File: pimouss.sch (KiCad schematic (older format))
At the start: 13 parts

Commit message: sch: Misc fixes
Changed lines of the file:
@@
 $Descr A4 11693 8268
 encoding utf-8
-Sheet 6 9
+Sheet 6 10
 Title "The Pimouss itself"
 Date "2019-03-19"
@@
 Text Label 3050 2000 0    50   ~ 0
 PWR_UP
-Text Label 3050 2100 0    50   ~ 0
+Text Label 3650 2100 2    50   ~ 0
 nRST
 NoConn ~ 2900 1900
@@
 Wire Wire Line
 	2900 2200 3650 2200
-Text Label 3050 2200 0    50   ~ 0
+Text Label 3650 2200 2    50   ~ 0
 nMR
 Wire Bus Line
@@
 Entry Wire Line
 	1450 1700 1550 1800
-Text Label 1100 1600 0    50   ~ 0
+Text Label 1050 1600 0    50   ~ 0
 PCIE_1X
 Wire Bus Line
@@
 Wire Bus Line
 	4150 3600 3750 3600
-Text Label 3800 3600 0    50   ~ 0
+Text Label 4150 3600 2    50   ~ 0
 PCIE_1X
 Entry Wire Line
@@
 Wire Bus Line
 	8050 2200 7650 2200
-Text Label 7700 2200 0    50   ~ 0
+Text Label 8050 2200 2    50   ~ 0
 PCIE_1X
 Entry Wire Line
@@
 Wire Bus Line
 	8050 1900 7650 1900
-Text Label 7700 1900 0    50   ~ 0
+Text Label 8050 1900 2    50   ~ 0
 PCIE_4X
 Entry Wire Line
@@
 Wire Bus Line
 	8050 3000 7650 3000
-Text Label 7700 3000 0    50   ~ 0
+Text Label 8050 3000 2    50   ~ 0
 PCIE_4X
 Entry Wire Line
@@
 Entry Wire Line
 	5350 2500 5450 2600
-Text Label 5000 2400 0    50   ~ 0
+Text Label 4950 2400 0    50   ~ 0
 PCIE_4X
 Entry Wire Line
@@
 Entry Wire Line
 	5350 4300 5450 4400
-Text Label 1100 2500 0    50   ~ 0
+Text Label 1050 2500 0    50   ~ 0
 QSGMII
 Wire Bus Line
 	4150 2200 3750 2200
-Text Label 3850 2200 0    50   ~ 0
+Text Label 4150 2200 2    50   ~ 0
 GPIO
 Entry Wire Line
@@
 Wire Bus Line
 	3750 2500 4150 2500
-Text Label 3850 2500 0    50   ~ 0
+Text Label 4150 2500 2    50   ~ 0
 MIIM
-Text Label 3850 2700 0    50   ~ 0
+Text Label 4150 2700 2    50   ~ 0
 GPIO
 NoConn ~ 2900 3200
@@
 Wire Wire Line
 	7550 1700 6800 1700
-Text Label 6950 1600 0    50   ~ 0
+Text Label 7550 1600 2    50   ~ 0
 BSTRAP_L
-Text Label 6950 1700 0    50   ~ 0
+Text Label 7550 1700 2    50   ~ 0
 BSTRAP_H
 NoConn ~ 6800 2900
@@
 Wire Bus Line
 	8050 2600 7650 2600
-Text Label 7750 2600 0    50   ~ 0
+Text Label 8050 2600 2    50   ~ 0
 UART
 Entry Wire Line
@@
 Wire Bus Line
 	8950 4100 8550 4100
-Text Label 8600 4100 0    50   ~ 0
+Text Label 8950 4100 2    50   ~ 0
 SMBUS
 Entry Wire Line
@@
 Wire Bus Line
 	8050 3400 7650 3400
-Text Label 7750 3400 0    50   ~ 0
+Text Label 8050 3400 2    50   ~ 0
 JTAG
 Entry Wire Line
@@
 Wire Bus Line
 	1900 5600 1500 5600
-Text Label 1550 5600 0    50   ~ 0
+Text Label 1900 5600 2    50   ~ 0
 PCIE_1X
 Wire Bus Line
 	1900 5700 1500 5700
-Text Label 1550 5700 0    50   ~ 0
+Text Label 1900 5700 2    50   ~ 0
 PCIE_4X
 Wire Bus Line
 	1900 5900 1500 5900
-Text Label 1550 5900 0    50   ~ 0
+Text Label 1900 5900 2    50   ~ 0
 QSGMII
 Wire Bus Line
 	1500 6000 1900 6000
-Text Label 1600 6000 0    50   ~ 0
+Text Label 1900 6000 2    50   ~ 0
 MIIM
 Wire Bus Line
 	1900 6200 1500 6200
-Text Label 1600 6200 0    50   ~ 0
+Text Label 1900 6200 2    50   ~ 0
 GPIO
 Wire Bus Line
 	1900 6300 1500 6300
-Text Label 1600 6300 0    50   ~ 0
+Text Label 1900 6300 2    50   ~ 0
 UART
 Wire Bus Line
 	1900 6400 1500 6400
-Text Label 1600 6400 0    50   ~ 0
+Text Label 1900 6400 2    50   ~ 0
 SDIO
 Wire Bus Line
 	1900 6500 1500 6500
-Text Label 1550 6500 0    50   ~ 0
+Text Label 1900 6500 2    50   ~ 0
 SMBUS
 Wire Bus Line
 	1900 6700 1500 6700
-Text Label 1600 6700 0    50   ~ 0
+Text Label 1900 6700 2    50   ~ 0
 JTAG
 Wire Wire Line
@@
 Wire Wire Line
 	1500 7000 1900 7000
-Text Label 1600 6900 0    50   ~ 0
+Text Label 1900 6900 2    50   ~ 0
 nRST
-Text Label 1600 7000 0    50   ~ 0
+Text Label 1900 7000 2    50   ~ 0
 nMR
 $Comp
@@
 Wire Wire Line
 	1500 7100 1900 7100
-Text Label 1550 7100 0    50   ~ 0
+Text Label 1900 7100 2    50   ~ 0
 BSTRAP
 $Comp
@@
 Wire Wire Line
 	6200 6100 5700 6100
-Text Label 5800 6000 0    50   ~ 0
+Text Label 6200 6000 2    50   ~ 0
 BSTRAP_L
-Text Label 5800 6100 0    50   ~ 0
+Text Label 6200 6100 2    50   ~ 0
 BSTRAP_H
 Wire Wire Line
@@
 Wire Wire Line
 	8150 3750 8200 3750
-Wire Bus Line
-	5350 2400 5350 4300
-Wire Bus Line
-	7650 3400 7650 4000
-Wire Bus Line
-	3750 2700 3750 3000
-Wire Bus Line
-	1450 2500 1450 2900
-Wire Bus Line
-	3750 2200 3750 2400
-Wire Bus Line
-	3750 3900 3750 4400
 Entry Wire Line
 	3650 4500 3750 4400
@@
 Entry Wire Line
 	3650 4200 3750 4100
-Text Label 3850 3900 0    50   ~ 0
+Text Label 4150 3900 2    50   ~ 0
 SDIO
 Wire Bus Line
@@
 Wire Wire Line
 	3650 4000 2900 4000
+Wire Bus Line
+	3750 2200 3750 2400
+Wire Bus Line
+	1450 2500 1450 2900
+Wire Bus Line
+	3750 2700 3750 3000
+Wire Bus Line
+	7650 3400 7650 4000
+Wire Bus Line
+	3750 3900 3750 4400
+Wire Bus Line
+	5350 2400 5350 4300
 $EndSCHEMATC

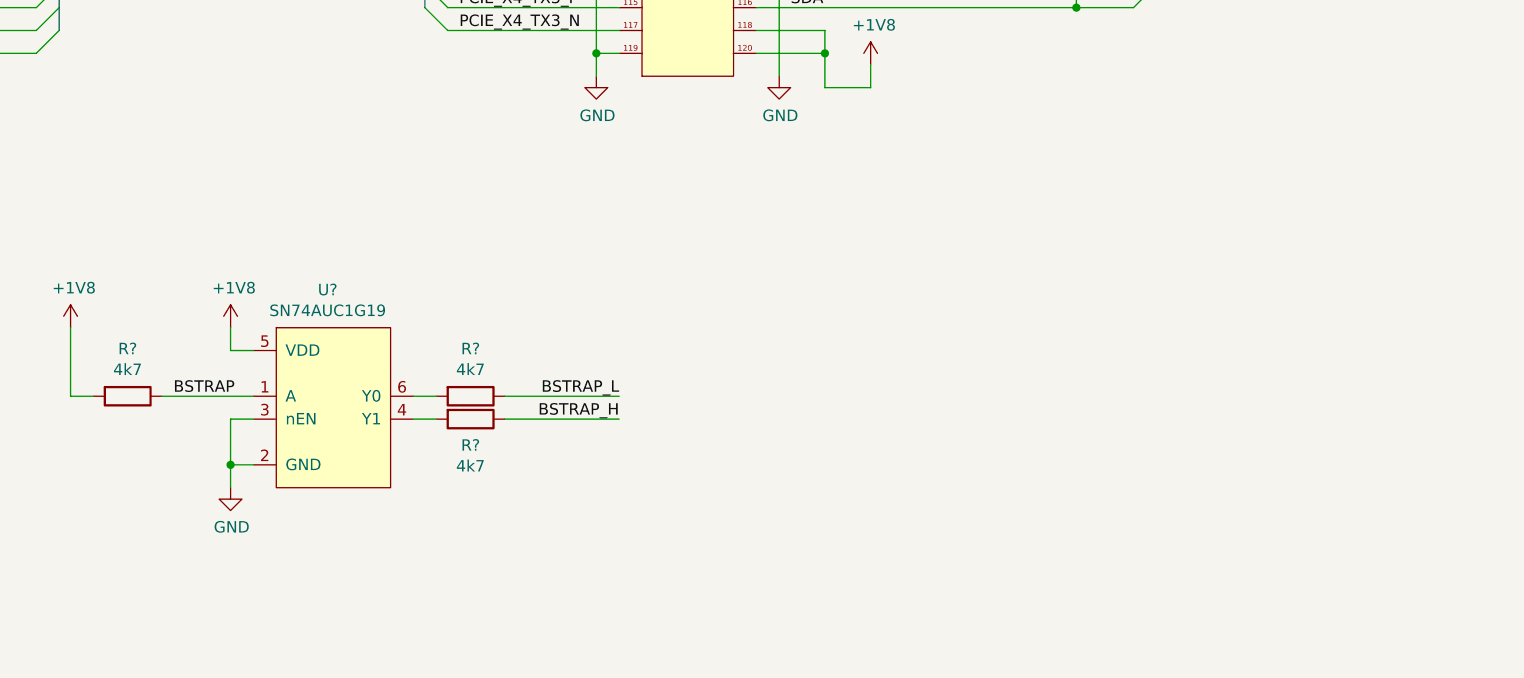
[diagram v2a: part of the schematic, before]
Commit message: sch: Add pimouss power connector
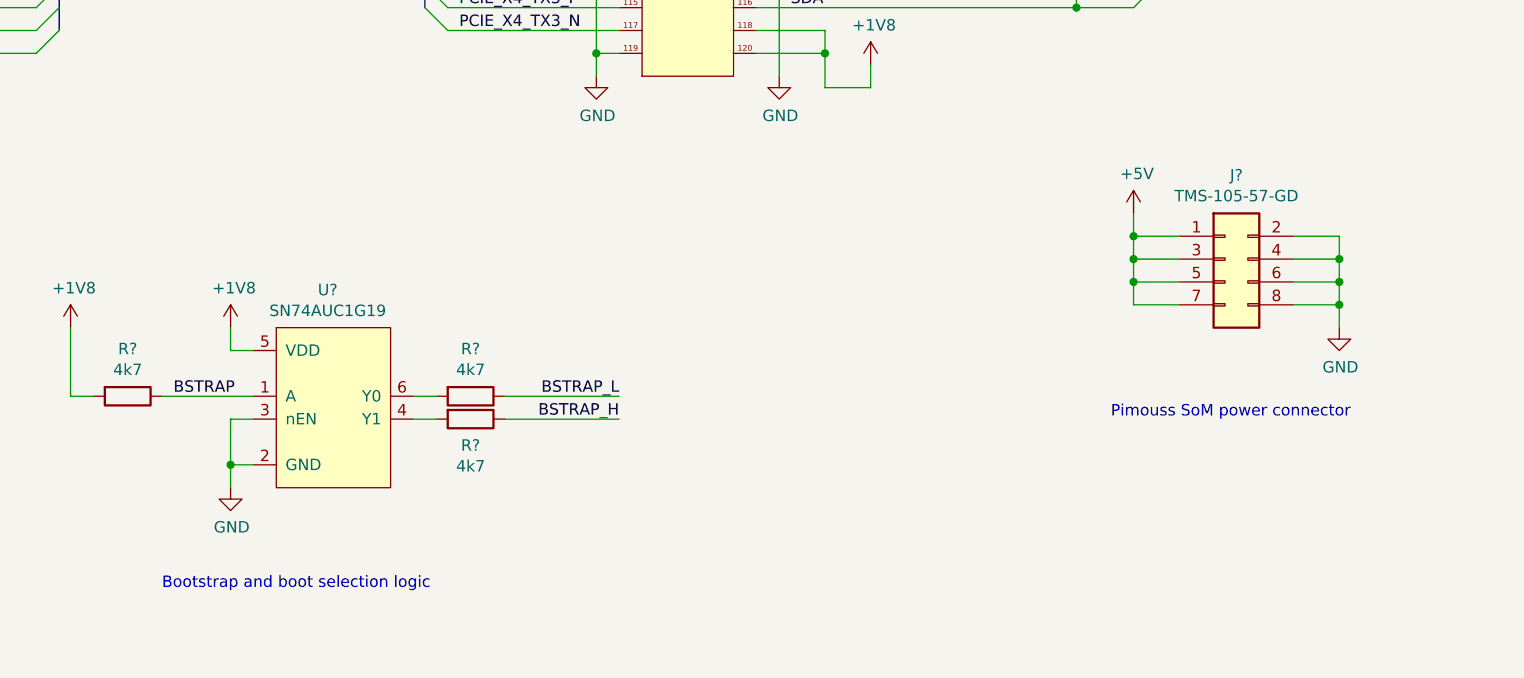
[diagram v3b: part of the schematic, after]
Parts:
- added J?: TMS-105-57-GD, pimouss-motherboard:TMS-105-57-G-D, symbol pimouss-motherboard:TMS-105-57-GD
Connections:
- net +5V: now also J?.1 (Pin_1), J?.3 (Pin_3), J?.5 (Pin_5), J?.7 (Pin_7)
- net GND: now also J?.2 (Pin_2), J?.4 (Pin_4), J?.6 (Pin_6), J?.8 (Pin_8)
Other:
- note added: "Bootstrap and boot selection logic\n"
- note added: "Pimouss SoM power connector"
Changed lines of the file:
@@
 Wire Wire Line
 	3650 4000 2900 4000
+$Comp
+L pimouss-motherboard:TMS-105-57-GD J?
+U 1 1 5DAB4506
+P 8800 5200
+F 0 "J?" H 8900 5367 50  0000 C CNN
+F 1 "TMS-105-57-GD" H 8900 5276 50  0000 C CNN
+F 2 "pimouss-motherboard:TMS-105-57-G-D" H 8800 5100 50  0001 C CNN
+F 3 "~" H 8850 5000 50  0001 C CNN
+	1    8800 5200
+	1    0    0    -1
+$EndComp
+$Comp
+L power:+5V #PWR?
+U 1 1 5DAB4C7D
+P 8450 5200
+F 0 "#PWR?" H 8450 5050 50  0001 C CNN
+F 1 "+5V" H 8465 5373 50  0000 C CNN
+F 2 "" H 8450 5200 50  0001 C CNN
+F 3 "" H 8450 5200 50  0001 C CNN
+	1    8450 5200
+	1    0    0    -1
+$EndComp
+$Comp
+L power:GND #PWR?
+U 1 1 5DAB4CAB
+P 9350 5700
+F 0 "#PWR?" H 9350 5450 50  0001 C CNN
+F 1 "GND" H 9355 5527 50  0000 C CNN
+F 2 "" H 9350 5700 50  0001 C CNN
+F 3 "" H 9350 5700 50  0001 C CNN
+	1    9350 5700
+	1    0    0    -1
+$EndComp
+Wire Wire Line
+	8450 5200 8450 5300
+Wire Wire Line
+	8450 5600 8650 5600
+Wire Wire Line
+	8450 5500 8650 5500
+Connection ~ 8450 5500
+Wire Wire Line
+	8450 5500 8450 5600
+Wire Wire Line
+	8450 5400 8650 5400
+Connection ~ 8450 5400
+Wire Wire Line
+	8450 5400 8450 5500
+Wire Wire Line
+	8450 5300 8650 5300
+Connection ~ 8450 5300
+Wire Wire Line
+	8450 5300 8450 5400
+Wire Wire Line
+	9150 5300 9350 5300
+Wire Wire Line
+	9350 5300 9350 5400
+Wire Wire Line
+	9150 5400 9350 5400
+Connection ~ 9350 5400
+Wire Wire Line
+	9350 5400 9350 5500
+Wire Wire Line
+	9150 5500 9350 5500
+Connection ~ 9350 5500
+Wire Wire Line
+	9350 5500 9350 5600
+Wire Wire Line
+	9150 5600 9350 5600
+Connection ~ 9350 5600
+Wire Wire Line
+	9350 5600 9350 5700
+Text Notes 9400 6100 2    50   ~ 0
+Pimouss SoM power connector
+Text Notes 4200 6850 0    50   ~ 0
+Bootstrap and boot selection logic\n
 Wire Bus Line
 	3750 2200 3750 2400

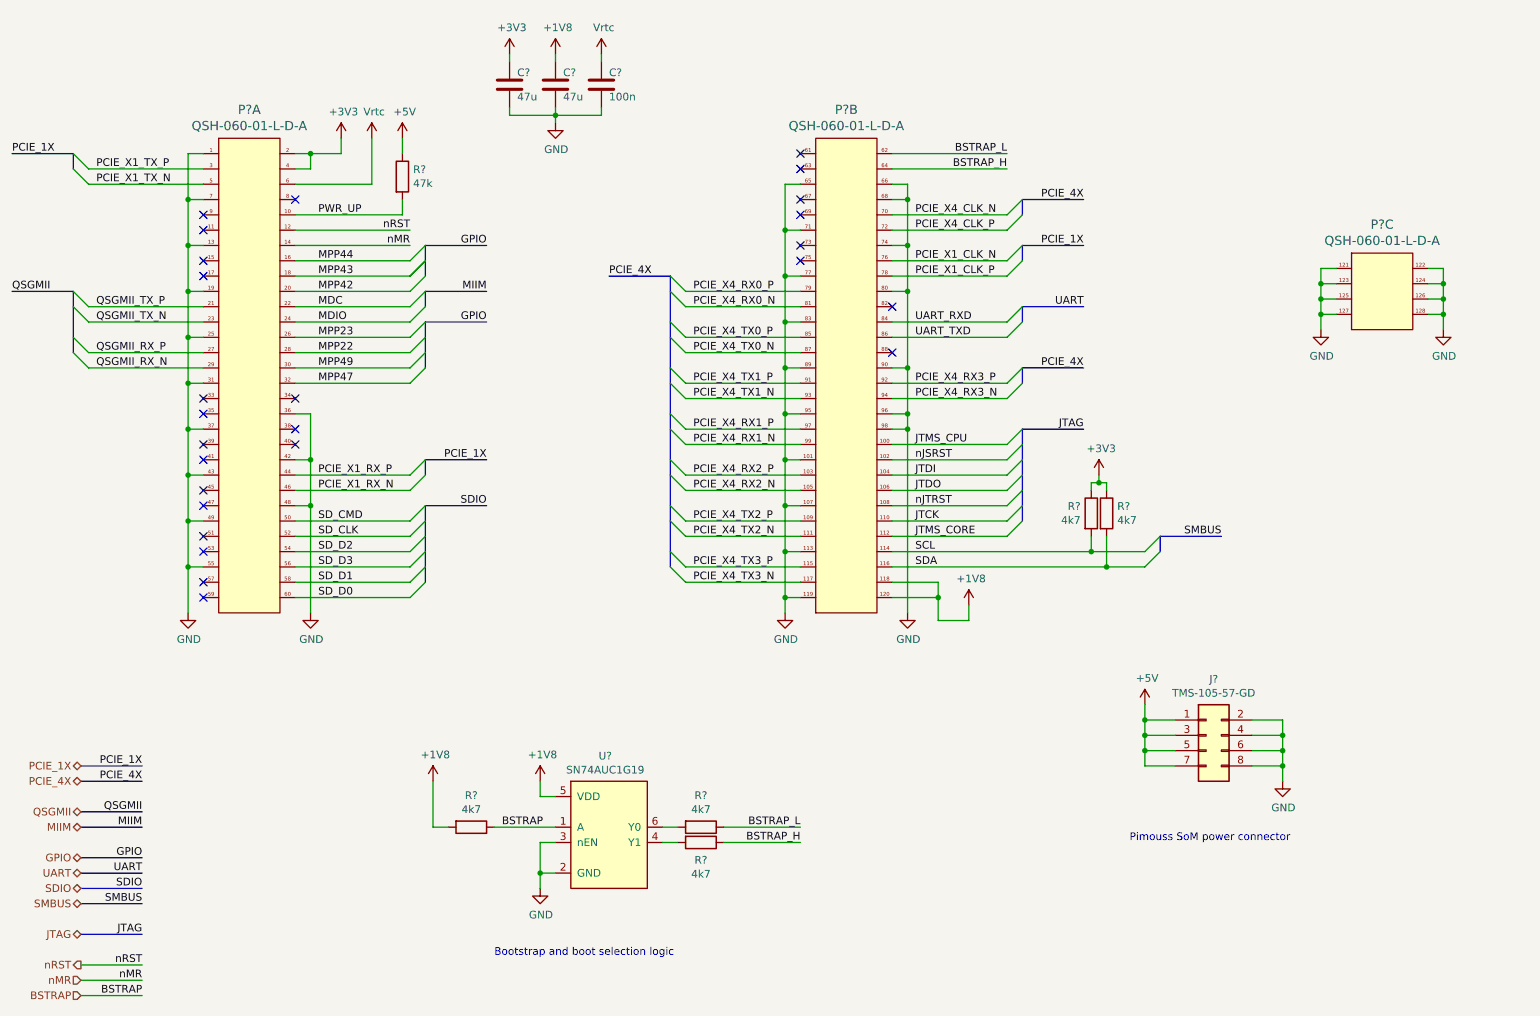
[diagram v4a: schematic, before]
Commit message: sch: Add connectors for JTAG and GPIO
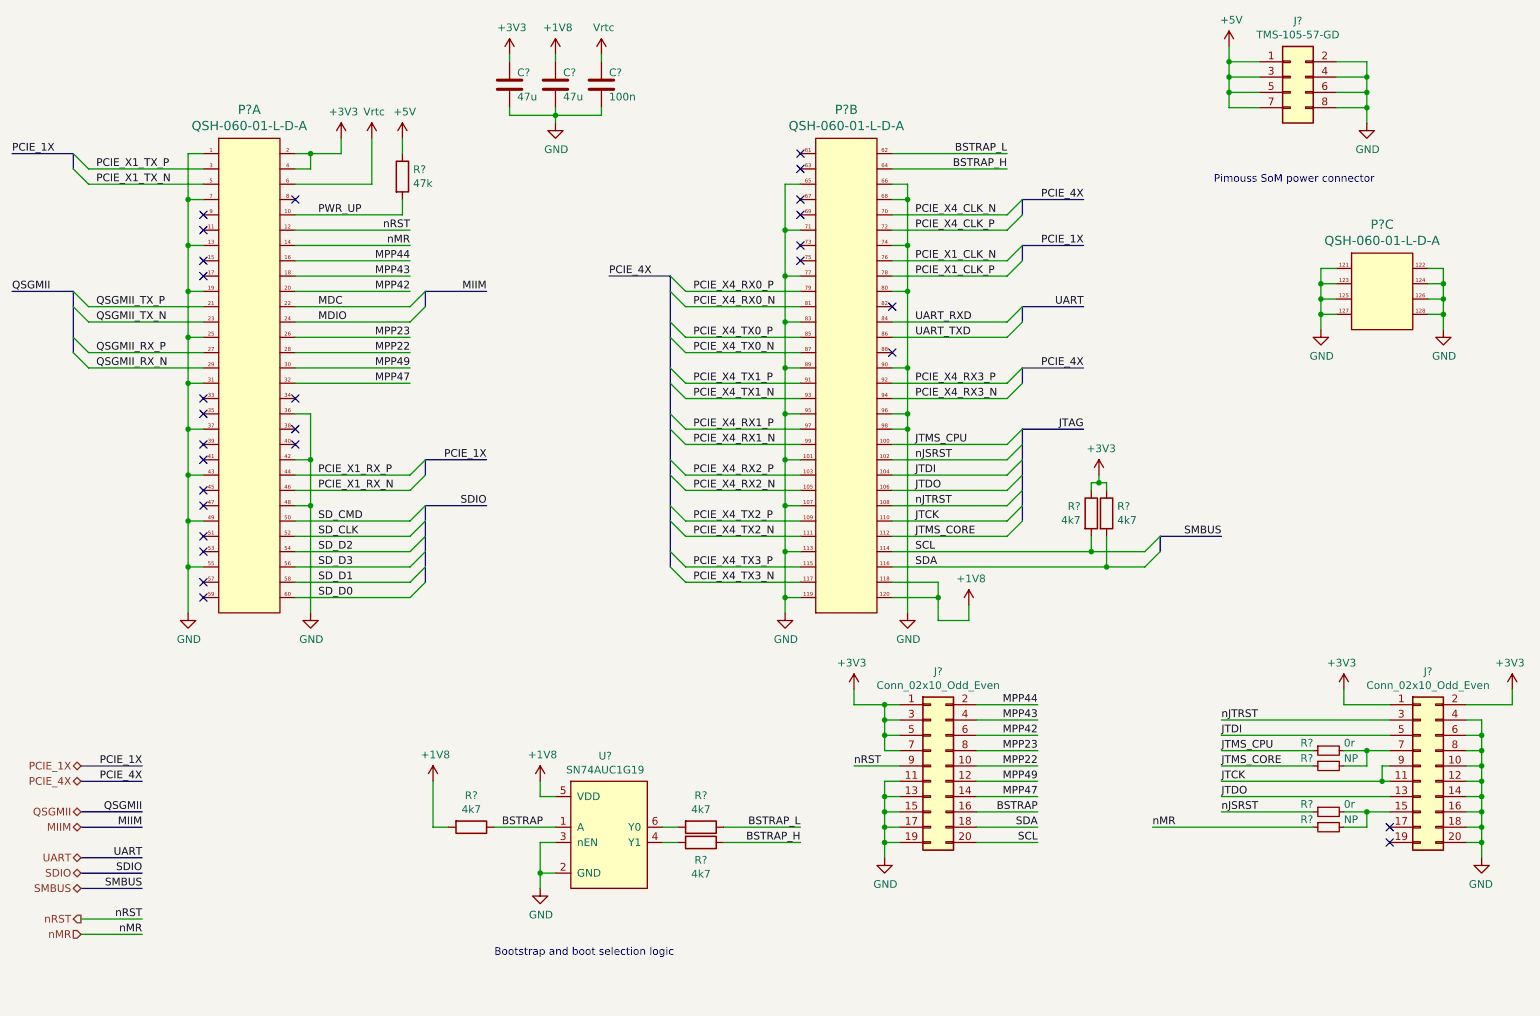
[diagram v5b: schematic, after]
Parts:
- added J? (x2): Conn_02x10_Odd_Even, symbol Connector_Generic:Conn_02x10_Odd_Even
- added R? (x2): 0r, symbol Device:R_Small
- added R? (x2): NP, symbol Device:R_Small
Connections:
- net +3V3: now also J?.1 (Pin_1), J?.1 (Pin_1), J?.2 (Pin_2), J?.3 (Pin_3), J?.5 (Pin_5), J?.7 (Pin_7)
- net BSTRAP: now also J?.16 (Pin_16)
- net GND: now also J?.10 (Pin_10), J?.11 (Pin_11), J?.12 (Pin_12), J?.13 (Pin_13), J?.14 (Pin_14), J?.15 (Pin_15), J?.16 (Pin_16), J?.17 (Pin_17), J?.18 (Pin_18), J?.19 (Pin_19), J?.20 (Pin_20), J?.4 (Pin_4), J?.6 (Pin_6), J?.8 (Pin_8)
- net JTCK: now also J?.11 (Pin_11), J?.9 (Pin_9)
- net JTDI: now also J?.5 (Pin_5)
- net JTDO: now also J?.13 (Pin_13)
- net JTMS_CORE: now also R?.1
- net JTMS_CPU: now also R?.1
- net MPP22: now also J?.10 (Pin_10)
- net MPP23: now also J?.8 (Pin_8)
- net MPP42: now also J?.6 (Pin_6)
- net MPP43: now also J?.4 (Pin_4)
- net MPP44: now also J?.2 (Pin_2)
- net MPP47: now also J?.14 (Pin_14)
- net MPP49: now also J?.12 (Pin_12)
- net SCL: now also J?.20 (Pin_20)
- net SDA: now also J?.18 (Pin_18)
- net nJSRST: now also R?.1
- net nJTRST: now also J?.3 (Pin_3)
- net nMR: now also R?.1
- net nRST: now also J?.9 (Pin_9)
- new net: J?.15 (Pin_15), R?.2, R?.2
- new net: J?.7 (Pin_7), R?.2, R?.2
- no-connect marks 26 -> 28
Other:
- moved on the sheet: J?
